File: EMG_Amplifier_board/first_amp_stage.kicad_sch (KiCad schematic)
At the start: 13 parts, among them U2 INA333xxDGK, U3 LPV821DBVR

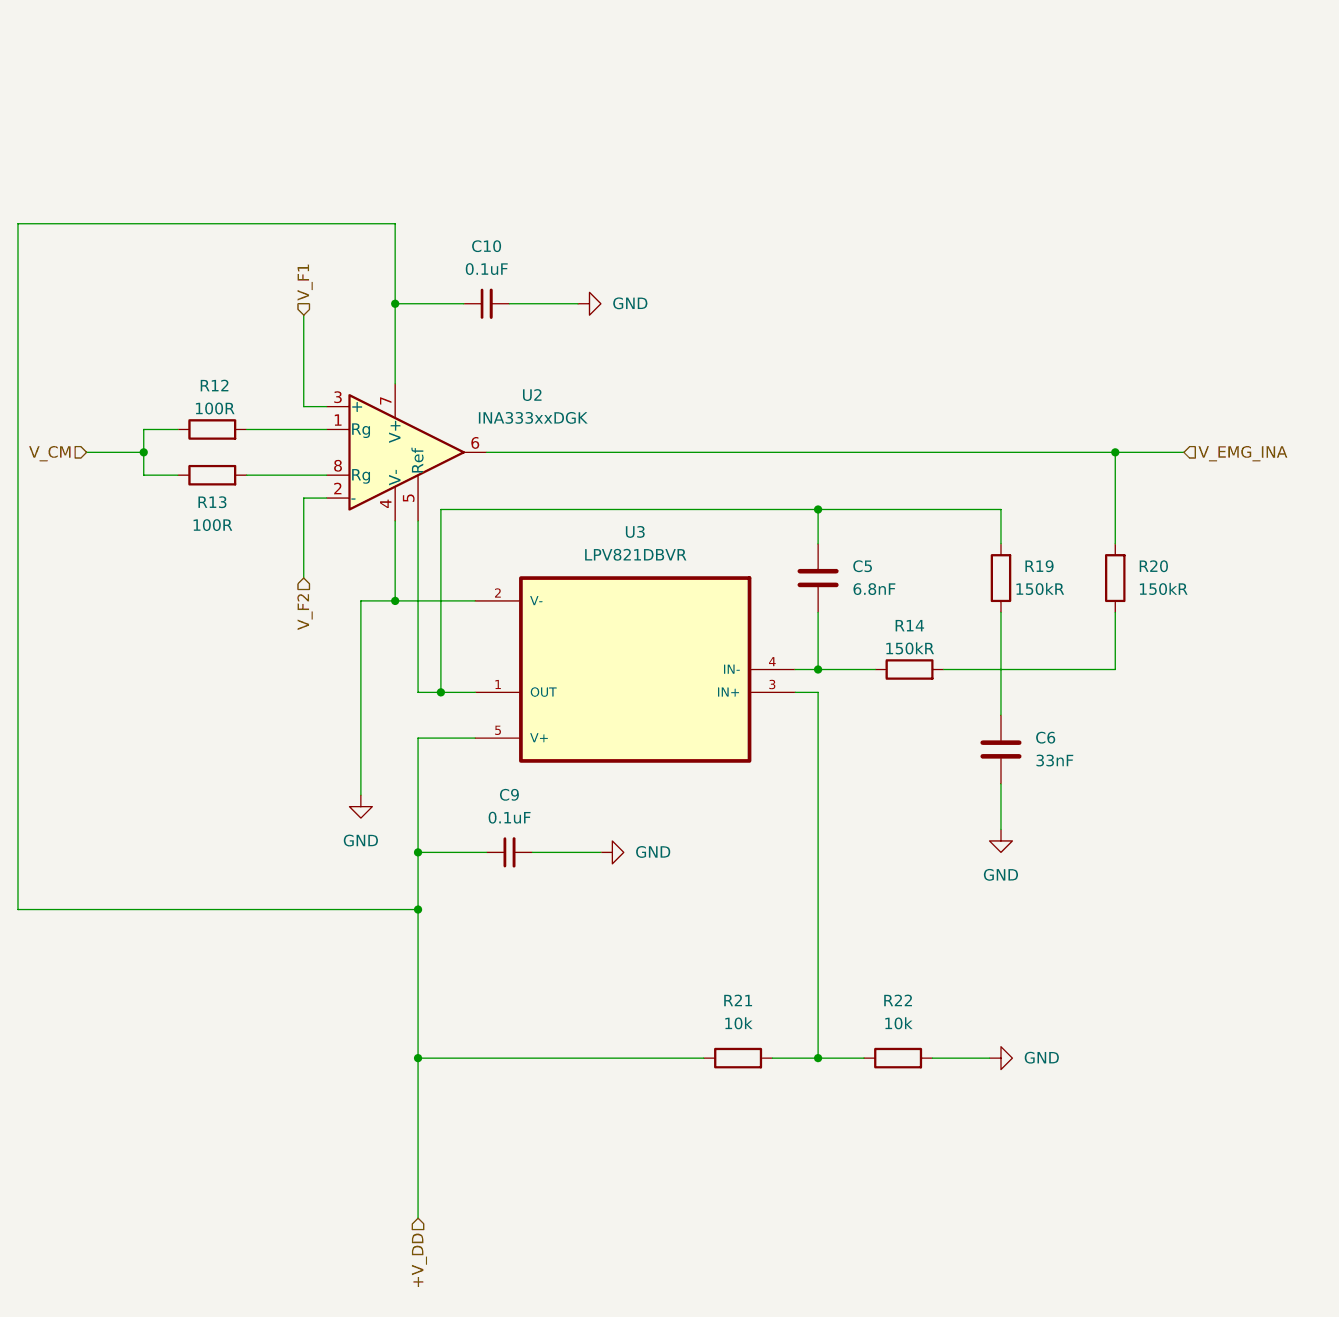
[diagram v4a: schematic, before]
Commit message: use one C10 capacitor instead of both C9 and C10
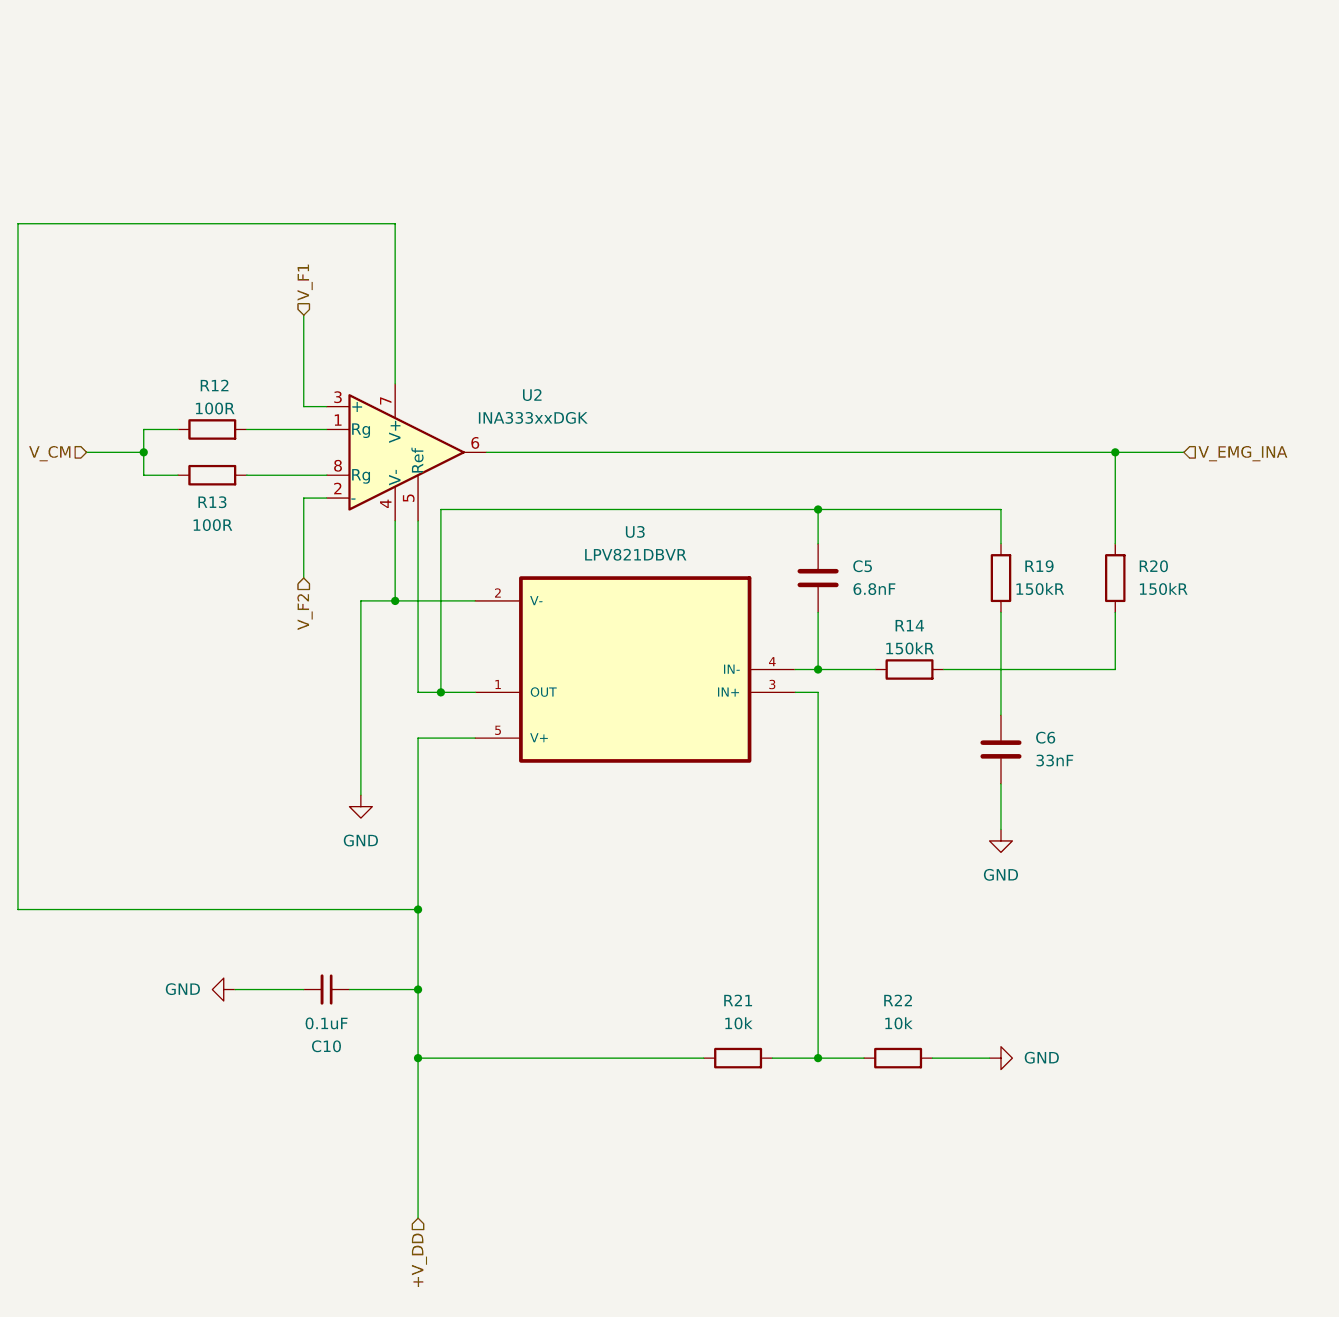
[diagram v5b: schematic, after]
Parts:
- removed C9: 0.1uF, Capacitor_SMD:C_0805_2012Metric, symbol Device:C_Small
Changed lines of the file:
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@@
-	)
-	(junction
-		(at 120.65 123.19)
-		(diameter 0)
-		(color 0 0 0 0)
 	)
 	(junction
@@
 	)
 	(junction
-		(at 118.11 62.23)
+		(at 120.65 138.43)
 		(diameter 0)
 		(color 0 0 0 0)
@@
 	(wire
 		(pts
-			(xy 133.35 123.19) (xy 140.97 123.19)
-		)
-		(stroke
-			(width 0)
-			(type default)
-		)
-	)
-	(wire
-		(pts
 			(xy 165.1 146.05) (xy 170.18 146.05)
 		)
@@
 	(wire
 		(pts
+			(xy 113.03 138.43) (xy 120.65 138.43)
+		)
+		(stroke
+			(width 0)
+			(type default)
+		)
+	)
+	(wire
+		(pts
 			(xy 107.95 73.66) (xy 110.49 73.66)
 		)
@@
 	(wire
 		(pts
-			(xy 118.11 62.23) (xy 118.11 71.12)
-		)
-		(stroke
-			(width 0)
-			(type default)
-		)
-	)
-	(wire
-		(pts
 			(xy 90.17 76.2) (xy 93.98 76.2)
 		)
@@
 	(wire
 		(pts
-			(xy 130.81 62.23) (xy 138.43 62.23)
-		)
-		(stroke
-			(width 0)
-			(type default)
-		)
-	)
-	(wire
-		(pts
-			(xy 128.27 123.19) (xy 120.65 123.19)
-		)
-		(stroke
-			(width 0)
-			(type default)
-		)
-	)
-	(wire
-		(pts
 			(xy 127 95.25) (xy 118.11 95.25)
 		)
@@
 	(wire
 		(pts
-			(xy 120.65 110.49) (xy 120.65 123.19)
-		)
-		(stroke
-			(width 0)
-			(type default)
-		)
-	)
-	(wire
-		(pts
 			(xy 90.17 81.28) (xy 93.98 81.28)
 		)
@@
 	(wire
 		(pts
-			(xy 120.65 123.19) (xy 120.65 129.54)
+			(xy 120.65 110.49) (xy 120.65 129.54)
 		)
 		(stroke
@@
 	(wire
 		(pts
-			(xy 120.65 129.54) (xy 120.65 146.05)
-		)
-		(stroke
-			(width 0)
-			(type default)
-		)
-	)
-	(wire
-		(pts
-			(xy 118.11 53.34) (xy 118.11 62.23)
+			(xy 120.65 129.54) (xy 120.65 138.43)
+		)
+		(stroke
+			(width 0)
+			(type default)
+		)
+	)
+	(wire
+		(pts
+			(xy 118.11 53.34) (xy 118.11 71.12)
 		)
 		(stroke
@@
 	(wire
 		(pts
-			(xy 125.73 62.23) (xy 118.11 62.23)
+			(xy 120.65 138.43) (xy 120.65 146.05)
 		)
 		(stroke
@@
 		(pts
 			(xy 76.2 129.54) (xy 76.2 53.34)
+		)
+		(stroke
+			(width 0)
+			(type default)
+		)
+	)
+	(wire
+		(pts
+			(xy 107.95 138.43) (xy 100.33 138.43)
 		)
 		(stroke
@@
 	(symbol
 		(lib_id "Device:C_Small")
-		(at 128.27 62.23 90)
+		(at 110.49 138.43 270)
 		(unit 1)
 		(exclude_from_sim no)
@@
 		(fields_autoplaced yes)
 		(property "Reference" "C10"
-			(at 128.2763 55.88 90)
+			(at 110.4837 144.78 90)
 			(effects
 				(font
@@
 		)
 		(property "Value" "0.1uF"
-			(at 128.2763 58.42 90)
+			(at 110.4837 142.24 90)
 			(effects
 				(font
@@
 		)
 		(property "Footprint" "Capacitor_SMD:C_0805_2012Metric"
-			(at 128.27 62.23 0)
+			(at 110.49 138.43 0)
 			(effects
 				(font
@@
 		)
 		(property "Datasheet" "~"
-			(at 128.27 62.23 0)
+			(at 110.49 138.43 0)
 			(effects
 				(font
@@
 		)
 		(property "Description" "Unpolarized capacitor, small symbol"
-			(at 128.27 62.23 0)
+			(at 110.49 138.43 0)
 			(effects
 				(font
@@
 	)
 	(symbol
-		(lib_id "power:GND")
-		(at 138.43 62.23 90)
-		(unit 1)
-		(exclude_from_sim no)
-		(in_bom yes)
-		(on_board yes)
-		(dnp no)
-		(fields_autoplaced yes)
-		(property "Reference" "#PWR020"
-			(at 144.78 62.23 0)
-			(effects
-				(font
-					(size 1.27 1.27)
-				)
-				(hide yes)
-			)
-		)
-		(property "Value" "GND"
-			(at 142.24 62.2299 90)
-			(effects
-				(font
-					(size 1.27 1.27)
-				)
-				(justify right)
-			)
-		)
-		(property "Footprint" ""
-			(at 138.43 62.23 0)
-			(effects
-				(font
-					(size 1.27 1.27)
-				)
-				(hide yes)
-			)
-		)
-		(property "Datasheet" ""
-			(at 138.43 62.23 0)
-			(effects
-				(font
-					(size 1.27 1.27)
-				)
-				(hide yes)
-			)
-		)
-		(property "Description" "Power symbol creates a global label with name \"GND\" , ground"
-			(at 138.43 62.23 0)
-			(effects
-				(font
-					(size 1.27 1.27)
-				)
-				(hide yes)
-			)
-		)
-		(pin "1"
-		)
-		(instances
-			(project "EMG_amplifier"
-				(path "/26861adc-1ddf-4c37-9f8b-8db1c0839771/190e8daf-ffdb-4cbc-86a8-05377b040767/ee6da384-2a51-46fd-9ef1-0e50994f466c"
-					(reference "#PWR020")
-					(unit 1)
-				)
-			)
-		)
-	)
-	(symbol
-		(lib_id "Device:C_Small")
-		(at 130.81 123.19 90)
-		(unit 1)
-		(exclude_from_sim no)
-		(in_bom yes)
-		(on_board yes)
-		(dnp no)
-		(fields_autoplaced yes)
-		(property "Reference" "C9"
-			(at 130.8163 116.84 90)
-			(effects
-				(font
-					(size 1.27 1.27)
-				)
-			)
-		)
-		(property "Value" "0.1uF"
-			(at 130.8163 119.38 90)
-			(effects
-				(font
-					(size 1.27 1.27)
-				)
-			)
-		)
-		(property "Footprint" "Capacitor_SMD:C_0805_2012Metric"
-			(at 130.81 123.19 0)
-			(effects
-				(font
-					(size 1.27 1.27)
-				)
-				(hide yes)
-			)
-		)
-		(property "Datasheet" "~"
-			(at 130.81 123.19 0)
-			(effects
-				(font
-					(size 1.27 1.27)
-				)
-				(hide yes)
-			)
-		)
-		(property "Description" "Unpolarized capacitor, small symbol"
-			(at 130.81 123.19 0)
-			(effects
-				(font
-					(size 1.27 1.27)
-				)
-				(hide yes)
-			)
-		)
-		(pin "1"
-		)
-		(pin "2"
-		)
-		(instances
-			(project "EMG_amplifier"
-				(path "/26861adc-1ddf-4c37-9f8b-8db1c0839771/190e8daf-ffdb-4cbc-86a8-05377b040767/ee6da384-2a51-46fd-9ef1-0e50994f466c"
-					(reference "C9")
-					(unit 1)
-				)
-			)
-		)
-	)
-	(symbol
 		(lib_id "Device:C")
 		(at 185.42 111.76 0)
@@
 				(path "/26861adc-1ddf-4c37-9f8b-8db1c0839771/190e8daf-ffdb-4cbc-86a8-05377b040767/ee6da384-2a51-46fd-9ef1-0e50994f466c"
 					(reference "#PWR015")
+					(unit 1)
+				)
+			)
+		)
+	)
+	(symbol
+		(lib_id "power:GND")
+		(at 100.33 138.43 270)
+		(unit 1)
+		(exclude_from_sim no)
+		(in_bom yes)
+		(on_board yes)
+		(dnp no)
+		(fields_autoplaced yes)
+		(property "Reference" "#PWR010"
+			(at 93.98 138.43 0)
+			(effects
+				(font
+					(size 1.27 1.27)
+				)
+				(hide yes)
+			)
+		)
+		(property "Value" "GND"
+			(at 96.52 138.4301 90)
+			(effects
+				(font
+					(size 1.27 1.27)
+				)
+				(justify right)
+			)
+		)
+		(property "Footprint" ""
+			(at 100.33 138.43 0)
+			(effects
+				(font
+					(size 1.27 1.27)
+				)
+				(hide yes)
+			)
+		)
+		(property "Datasheet" ""
+			(at 100.33 138.43 0)
+			(effects
+				(font
+					(size 1.27 1.27)
+				)
+				(hide yes)
+			)
+		)
+		(property "Description" "Power symbol creates a global label with name \"GND\" , ground"
+			(at 100.33 138.43 0)
+			(effects
+				(font
+					(size 1.27 1.27)
+				)
+				(hide yes)
+			)
+		)
+		(pin "1"
+		)
+		(instances
+			(project "EMG_amplifier"
+				(path "/26861adc-1ddf-4c37-9f8b-8db1c0839771/190e8daf-ffdb-4cbc-86a8-05377b040767/ee6da384-2a51-46fd-9ef1-0e50994f466c"
+					(reference "#PWR010")
 					(unit 1)
 				)
@@
 					(unit 1)
 				)
-			)
-		)
-	)
-	(symbol
-		(lib_id "power:GND")
-		(at 140.97 123.19 90)
-		(unit 1)
-		(exclude_from_sim no)
-		(in_bom yes)
-		(on_board yes)
-		(dnp no)
-		(fields_autoplaced yes)
-		(property "Reference" "#PWR013"
-			(at 147.32 123.19 0)
-			(effects
-				(font
-					(size 1.27 1.27)
-				)
-				(hide yes)
-			)
-		)
-		(property "Value" "GND"
-			(at 144.78 123.1899 90)
-			(effects
-				(font
-					(size 1.27 1.27)
-				)
-				(justify right)
-			)
-		)
-		(property "Footprint" ""
-			(at 140.97 123.19 0)
-			(effects
-				(font
-					(size 1.27 1.27)
-				)
-				(hide yes)
-			)
-		)
-		(property "Datasheet" ""
-			(at 140.97 123.19 0)
-			(effects
-				(font
-					(size 1.27 1.27)
-				)
-				(hide yes)
-			)
-		)
-		(property "Description" "Power symbol creates a global label with name \"GND\" , ground"
-			(at 140.97 123.19 0)
-			(effects
-				(font
-					(size 1.27 1.27)
-				)
-				(hide yes)
-			)
-		)
-		(pin "1"
-		)
-		(instances
-			(project "EMG_amplifier"
-				(path "/26861adc-1ddf-4c37-9f8b-8db1c0839771/190e8daf-ffdb-4cbc-86a8-05377b040767/ee6da384-2a51-46fd-9ef1-0e50994f466c"
-					(reference "#PWR013")
-					(unit 1)
-				)

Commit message: before working on one-sided design
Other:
- moved on the sheet: C10, C5, C6, R12, R13, R14, R19, R20, R21, R22, U2, U3

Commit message: first revision
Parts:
- R12, R13: value 100R -> 100
- R14, R19, R20: value 150kR -> 150k
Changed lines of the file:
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@@
 			)
 		)
-		(property "Value" "100R"
+		(property "Value" "100"
 			(at 99.06 64.008 90)
 			(effects
@@
 			)
 		)
-		(property "Value" "150kR"
+		(property "Value" "150k"
 			(at 201.93 71.1199 0)
 			(effects
@@
 			)
 		)
-		(property "Value" "150kR"
+		(property "Value" "150k"
 			(at 188.214 71.12 0)
 			(effects
@@
 			)
 		)
-		(property "Value" "150kR"
+		(property "Value" "150k"
 			(at 176.53 77.724 90)
 			(effects
@@
 			)
 		)
-		(property "Value" "100R"
+		(property "Value" "100"
 			(at 99.314 51.054 90)
 			(effects
